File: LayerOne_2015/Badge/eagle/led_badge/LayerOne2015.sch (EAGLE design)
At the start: 72 parts, among them IC2 PQ1X331M2ZP-3V3-LDO-SOT-23-5, Q1 BSS138

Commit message: 
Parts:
- removed Q1: BSS138, SparkFun:MOSFET-NCHANNELSMD
- removed R5, R6: 10K, SparkFun:RESISTOR0805-RES
- added IC9: M74VHC1GT125DF2G, 74xx-little-de:74AHC1G125DCK
- added JP4: (no value), SparkFun:M07
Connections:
- removed net P1_5_5V: Q1.D, R6.2
- removed net P4_VDD: D1.C, IC2.VC, IC2.VIN, JP2.1, R6.1
- new net N$29: JP4.7, U$1.P0_0
- new net N$30: JP4.6, U$1.P0_1
- new net N$31: JP4.5, U$1.P0_2
- new net N$32: JP4.4, U$1.P0_3
- new net N$33: JP4.3, U$1.P0_4
- new net N$34: JP4.2, U$1.P0_5
- new net N$35: JP4.1, U$1.P0_6
- new net VCC: D1.C, IC2.VC, IC2.VIN, JP2.1
- net 3.3V: no longer Q1.G, R5.1
- net DIN: now also IC9A.O
- net GND: now also IC9A.OE
- net P1_5_3V: now also IC9A.I; no longer Q1.S, R5.2
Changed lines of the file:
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@@
 <?xml version="1.0" encoding="utf-8"?>
 <!DOCTYPE eagle SYSTEM "eagle.dtd">
-<eagle version="7.1.0">
+<eagle version="7.2.0">
 <drawing>
 <settings>
@@
 <part name="GND10" library="SparkFun-Aesthetics" deviceset="GND" device=""/>
 <part name="JP3" library="SparkFun-Connectors" deviceset="M05" device="PTH"/>
-<part name="Q1" library="SparkFun" deviceset="MOSFET-NCHANNEL" device="SMD" value="BSS138"/>
-<part name="R5" library="SparkFun" deviceset="RESISTOR" device="0805-RES" value="10K"/>
-<part name="R6" library="SparkFun" deviceset="RESISTOR" device="0805-RES" value="10K"/>
 <part name="BAT1" library="tvbgone-adj" deviceset="BATTERY" device="CR123A" value="CR123A"/>
 <part name="BAT2" library="tvbgone-adj" deviceset="BATTERY" device="CR123A" value="CR123A"/>
 <part name="GND12" library="supply1" deviceset="GND" device=""/>
 <part name="D1" library="SparkFun-DiscreteSemi" deviceset="DIODE" device="SMA"/>
+<part name="IC9" library="74xx-little-de" deviceset="74*1G125" device="DCK" technology="AHC" value="M74VHC1GT125DF2G ">
+<attribute name="DIGIKEY-ND" value="M74VHC1GT125DF1GOSCT-ND"/>
+<attribute name="MOUSER" value="863-M74VHC1GT125DF2G"/>
+<attribute name="PARTNO" value="M74VHC1GT125DF2G"/>
+</part>
+<part name="GND11" library="SparkFun-Aesthetics" deviceset="GND" device=""/>
+<part name="JP4" library="SparkFun" deviceset="M07" device=""/>
 </parts>
 <sheets>
@@
 <instance part="C23" gate="G$1" x="99.06" y="71.12"/>
 <instance part="GND1" gate="1" x="99.06" y="63.5"/>
-<instance part="C24" gate="G$1" x="124.46" y="40.64"/>
-<instance part="R1" gate="G$1" x="124.46" y="53.34" rot="R90"/>
-<instance part="GND2" gate="1" x="124.46" y="33.02"/>
+<instance part="C24" gate="G$1" x="134.62" y="40.64"/>
+<instance part="R1" gate="G$1" x="134.62" y="53.34" rot="R90"/>
+<instance part="GND2" gate="1" x="134.62" y="33.02"/>
 <instance part="C25" gate="G$1" x="119.38" y="78.74"/>
 <instance part="R2" gate="G$1" x="119.38" y="91.44" rot="R90"/>
@@
 <instance part="GND10" gate="1" x="25.4" y="68.58"/>
 <instance part="JP3" gate="G$1" x="-7.62" y="53.34"/>
-<instance part="Q1" gate="G$1" x="-15.24" y="-5.08" smashed="yes" rot="R270">
-<attribute name="NAME" x="-19.05" y="-0.254" size="1.778" layer="95"/>
-<attribute name="VALUE" x="-20.574" y="-10.668" size="1.778" layer="96"/>
-</instance>
-<instance part="R5" gate="G$1" x="-22.86" y="2.54" rot="R270"/>
-<instance part="R6" gate="G$1" x="-7.62" y="2.54" rot="R270"/>
 <instance part="BAT1" gate="G$1" x="-27.94" y="96.52" smashed="yes">
 <attribute name="NAME" x="-31.75" y="101.6" size="1.778" layer="95"/>
@@
 </instance>
 <instance part="D1" gate="G$1" x="-50.8" y="96.52" rot="R180"/>
+<instance part="IC9" gate="A" x="-25.4" y="0" smashed="yes">
+<attribute name="NAME" x="-22.86" y="3.175" size="1.778" layer="95"/>
+<attribute name="VALUE" x="-35.56" y="-7.62" size="1.778" layer="96"/>
+<attribute name="MOUSER" x="-25.4" y="0" size="1.778" layer="96" display="off"/>
+<attribute name="PARTNO" x="-25.4" y="0" size="1.778" layer="96" display="off"/>
+<attribute name="DIGIKEY-ND" x="-25.4" y="0" size="1.778" layer="96" display="off"/>
+</instance>
+<instance part="GND11" gate="1" x="-25.4" y="15.24" rot="R180"/>
+<instance part="JP4" gate="G$1" x="111.76" y="48.26" rot="R180"/>
 </instances>
 <busses>
@@
 <pinref part="C24" gate="G$1" pin="2"/>
 <pinref part="GND2" gate="1" pin="GND"/>
-<wire x1="124.46" y1="35.56" x2="124.46" y2="38.1" width="0.1524" layer="91"/>
+<wire x1="134.62" y1="35.56" x2="134.62" y2="38.1" width="0.1524" layer="91"/>
 </segment>
 <segment>
@@
 <pinref part="GND12" gate="1" pin="GND"/>
 </segment>
+<segment>
+<pinref part="IC9" gate="A" pin="OE"/>
+<pinref part="GND11" gate="1" pin="GND"/>
+<wire x1="-25.4" y1="12.7" x2="-25.4" y2="7.62" width="0.1524" layer="91"/>
+</segment>
 </net>
 <net name="GPIO2_3V" class="0">
@@
 <wire x1="0" y1="48.26" x2="7.62" y2="48.26" width="0.2032" layer="91"/>
 <label x="7.62" y="48.26" size="1.778" layer="95"/>
-</segment>
-<segment>
-<wire x1="-22.86" y1="7.62" x2="-22.86" y2="10.16" width="0.1524" layer="91"/>
-<wire x1="-22.86" y1="10.16" x2="-22.86" y2="12.7" width="0.1524" layer="91"/>
-<wire x1="-15.24" y1="2.54" x2="-15.24" y2="10.16" width="0.1524" layer="91"/>
-<wire x1="-15.24" y1="10.16" x2="-22.86" y2="10.16" width="0.1524" layer="91"/>
-<junction x="-22.86" y="10.16"/>
-<pinref part="R5" gate="G$1" pin="1"/>
-<pinref part="Q1" gate="G$1" pin="G"/>
-<label x="-22.86" y="12.7" size="1.778" layer="95" rot="R90"/>
 </segment>
 </net>
@@
 <pinref part="C24" gate="G$1" pin="1"/>
 <pinref part="R1" gate="G$1" pin="1"/>
-<wire x1="124.46" y1="48.26" x2="124.46" y2="45.72" width="0.1524" layer="91"/>
+<wire x1="134.62" y1="48.26" x2="134.62" y2="45.72" width="0.1524" layer="91"/>
 </segment>
 </net>
@@
 <segment>
 <pinref part="U$1" gate="G$1" pin="P4_3"/>
-<wire x1="86.36" y1="35.56" x2="93.98" y2="35.56" width="0.1524" layer="91"/>
-<label x="93.98" y="35.56" size="1.778" layer="95" xref="yes"/>
+<wire x1="86.36" y1="35.56" x2="88.9" y2="35.56" width="0.1524" layer="91"/>
+<label x="88.9" y="35.56" size="1.778" layer="95" xref="yes"/>
 </segment>
 </net>
@@
 <segment>
 <pinref part="R1" gate="G$1" pin="2"/>
-<wire x1="124.46" y1="58.42" x2="124.46" y2="60.96" width="0.1524" layer="91"/>
-<wire x1="124.46" y1="60.96" x2="116.84" y2="60.96" width="0.1524" layer="91"/>
+<wire x1="134.62" y1="58.42" x2="134.62" y2="60.96" width="0.1524" layer="91"/>
+<wire x1="134.62" y1="60.96" x2="116.84" y2="60.96" width="0.1524" layer="91"/>
 <label x="116.84" y="60.96" size="1.778" layer="95" rot="R180" xref="yes"/>
 </segment>
@@
 </segment>
 <segment>
-<pinref part="Q1" gate="G$1" pin="S"/>
-<wire x1="-20.32" y1="-5.08" x2="-22.86" y2="-5.08" width="0.1524" layer="91"/>
-<pinref part="R5" gate="G$1" pin="2"/>
-<wire x1="-22.86" y1="-5.08" x2="-30.48" y2="-5.08" width="0.1524" layer="91"/>
-<wire x1="-22.86" y1="-2.54" x2="-22.86" y2="-5.08" width="0.1524" layer="91"/>
-<junction x="-22.86" y="-5.08"/>
-<label x="-30.48" y="-5.08" size="1.27" layer="95" rot="R90" xref="yes"/>
+<wire x1="-30.48" y1="0" x2="-38.1" y2="0" width="0.1524" layer="91"/>
+<pinref part="IC9" gate="A" pin="I"/>
+<label x="-50.8" y="0" size="1.778" layer="95"/>
 </segment>
 </net>
@@
 </segment>
 </net>
-<net name="P4_VDD" class="0">
+<net name="VCC" class="0">
 <segment>
 <pinref part="IC2" gate="G$1" pin="VIN"/>
@@
 </segment>
 <segment>
-<wire x1="-7.62" y1="7.62" x2="-7.62" y2="12.7" width="0.1524" layer="91"/>
-<pinref part="R6" gate="G$1" pin="1"/>
-<label x="-7.62" y="12.7" size="1.778" layer="95" rot="R90"/>
-</segment>
-<segment>
 <pinref part="JP2" gate="G$1" pin="1"/>
 <wire x1="149.86" y1="40.64" x2="149.86" y2="33.02" width="0.2032" layer="91"/>
@@
 <wire x1="-55.88" y1="96.52" x2="-55.88" y2="81.28" width="0.2032" layer="91"/>
 <label x="-55.88" y="81.28" size="1.778" layer="95" rot="R270" xref="yes"/>
-</segment>
-</net>
-<net name="P1_5_5V" class="0">
-<segment>
-<pinref part="Q1" gate="G$1" pin="D"/>
-<wire x1="-10.16" y1="-5.08" x2="-7.62" y2="-5.08" width="0.1524" layer="91"/>
-<pinref part="R6" gate="G$1" pin="2"/>
-<wire x1="-7.62" y1="-5.08" x2="-5.08" y2="-5.08" width="0.1524" layer="91"/>
-<wire x1="-7.62" y1="-2.54" x2="-7.62" y2="-5.08" width="0.1524" layer="91"/>
-<junction x="-7.62" y="-5.08"/>
-<label x="-5.08" y="-5.08" size="1.27" layer="95" xref="yes"/>
 </segment>
 </net>
@@
 <label x="152.4" y="22.86" size="1.778" layer="95" rot="R270"/>
 </segment>
+<segment>
+<wire x1="-17.78" y1="0" x2="-10.16" y2="0" width="0.1524" layer="91"/>
+<pinref part="IC9" gate="A" pin="O"/>
+<label x="-10.16" y="0" size="1.778" layer="95"/>
+</segment>
+</net>
+<net name="N$29" class="0">
+<segment>
+<pinref part="U$1" gate="G$1" pin="P0_0"/>
+<wire x1="86.36" y1="38.1" x2="106.68" y2="38.1" width="0.1524" layer="91"/>
+<pinref part="JP4" gate="G$1" pin="7"/>
+</segment>
+</net>
+<net name="N$30" class="0">
+<segment>
+<pinref part="U$1" gate="G$1" pin="P0_1"/>
+<wire x1="86.36" y1="40.64" x2="106.68" y2="40.64" width="0.1524" layer="91"/>
+<pinref part="JP4" gate="G$1" pin="6"/>
+</segment>
+</net>
+<net name="N$31" class="0">
+<segment>
+<pinref part="U$1" gate="G$1" pin="P0_2"/>
+<wire x1="86.36" y1="43.18" x2="106.68" y2="43.18" width="0.1524" layer="91"/>
+<pinref part="JP4" gate="G$1" pin="5"/>
+</segment>
+</net>
+<net name="N$32" class="0">
+<segment>
+<pinref part="U$1" gate="G$1" pin="P0_3"/>
+<wire x1="86.36" y1="45.72" x2="106.68" y2="45.72" width="0.1524" layer="91"/>
+<pinref part="JP4" gate="G$1" pin="4"/>
+</segment>
+</net>
+<net name="N$33" class="0">
+<segment>
+<pinref part="U$1" gate="G$1" pin="P0_4"/>
+<wire x1="86.36" y1="48.26" x2="106.68" y2="48.26" width="0.1524" layer="91"/>
+<pinref part="JP4" gate="G$1" pin="3"/>
+</segment>
+</net>
+<net name="N$34" class="0">
+<segment>
+<pinref part="U$1" gate="G$1" pin="P0_5"/>
+<wire x1="86.36" y1="50.8" x2="106.68" y2="50.8" width="0.1524" layer="91"/>
+<pinref part="JP4" gate="G$1" pin="2"/>
+</segment>
+</net>
+<net name="N$35" class="0">
+<segment>
+<pinref part="U$1" gate="G$1" pin="P0_6"/>
+<wire x1="86.36" y1="53.34" x2="106.68" y2="53.34" width="0.1524" layer="91"/>
+<pinref part="JP4" gate="G$1" pin="1"/>
+</segment>
 </net>
 </nets>
 </sheet>
-<sheet>
-<plain>
-</plain>
-<instances>
-</instances>
-<busses>
-</busses>
-<nets>
-</nets>
-</sheet>

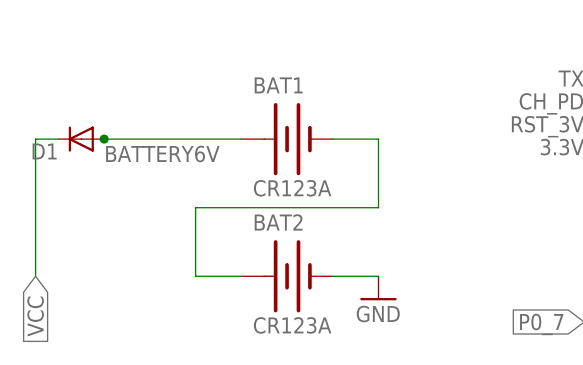
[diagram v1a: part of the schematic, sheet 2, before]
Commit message: 
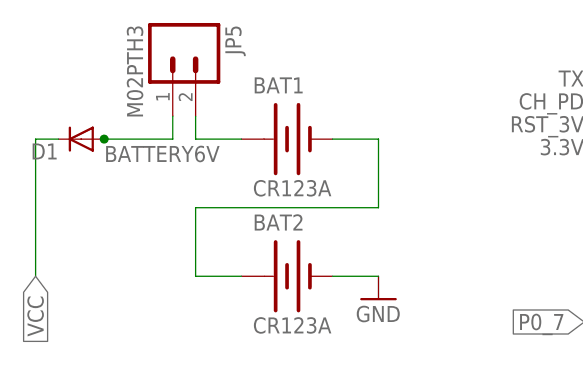
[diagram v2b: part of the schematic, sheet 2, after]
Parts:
- added JP5: M02PTH3, SparkFun-Connectors:M02PTH3
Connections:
- removed net VDD: C1.1, C10.1, C11.1, C12.1, C13.1, C14.1, C15.1, C16.1, C17.1, C18.1, C19.1, C2.1, C20.1, C21.1, C22.1, C3.1, C4.1, C5.1, C6.1, C7.1, C8.1, C9.1, L1.VDD, L10.VDD, L11.VDD, L12.VDD, L13.VDD, L14.VDD, L15.VDD, L16.VDD, L17.VDD, L18.VDD, L19.VDD, L2.VDD, L20.VDD, L21.VDD, L22.VDD, L3.VDD, L4.VDD, L5.VDD, L6.VDD, L7.VDD, L8.VDD, L9.VDD
- new net N$36: BAT1.+, JP5.2
- net BATTERY6V: now also JP5.1; no longer BAT1.+
- net VCC: now also C1.1, C10.1, C11.1, C12.1, C13.1, C14.1, C15.1, C16.1, C17.1, C18.1, C19.1, C2.1, C20.1, C21.1, C22.1, C3.1, C4.1, C5.1, C6.1, C7.1, C8.1, C9.1, L1.VDD, L10.VDD, L11.VDD, L12.VDD, L13.VDD, L14.VDD, L15.VDD, L16.VDD, L17.VDD, L18.VDD, L19.VDD, L2.VDD, L20.VDD, L21.VDD, L22.VDD, L3.VDD, L4.VDD, L5.VDD, L6.VDD, L7.VDD, L8.VDD, L9.VDD
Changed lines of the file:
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@@
 <part name="GND11" library="SparkFun-Aesthetics" deviceset="GND" device=""/>
 <part name="JP4" library="SparkFun" deviceset="M07" device=""/>
+<part name="JP5" library="SparkFun-Connectors" deviceset="M02" device="PTH3"/>
 </parts>
 <sheets>
@@
 </segment>
 </net>
-<net name="VDD" class="0">
+<net name="N$19" class="0">
+<segment>
+<pinref part="L22" gate="G$1" pin="DOUT"/>
+<pinref part="JP1-DOUT" gate="G$1" pin="1"/>
+<wire x1="25.4" y1="7.62" x2="43.18" y2="7.62" width="0.2032" layer="91"/>
+</segment>
+</net>
+<net name="N$25" class="0">
+<segment>
+<pinref part="L10" gate="G$1" pin="DOUT"/>
+<wire x1="152.4" y1="83.82" x2="157.48" y2="83.82" width="0.2032" layer="91"/>
+<wire x1="157.48" y1="83.82" x2="157.48" y2="66.04" width="0.2032" layer="91"/>
+<wire x1="157.48" y1="66.04" x2="-10.16" y2="66.04" width="0.2032" layer="91"/>
+<wire x1="-10.16" y1="66.04" x2="-10.16" y2="45.72" width="0.2032" layer="91"/>
+<pinref part="L11" gate="G$1" pin="DIN"/>
+<wire x1="-10.16" y1="45.72" x2="-2.54" y2="45.72" width="0.2032" layer="91"/>
+</segment>
+</net>
+<net name="N$26" class="0">
+<segment>
+<pinref part="L20" gate="G$1" pin="DOUT"/>
+<wire x1="152.4" y1="45.72" x2="154.94" y2="45.72" width="0.2032" layer="91"/>
+<wire x1="154.94" y1="45.72" x2="154.94" y2="27.94" width="0.2032" layer="91"/>
+<wire x1="154.94" y1="27.94" x2="-7.62" y2="27.94" width="0.2032" layer="91"/>
+<wire x1="-7.62" y1="27.94" x2="-7.62" y2="7.62" width="0.2032" layer="91"/>
+<pinref part="L21" gate="G$1" pin="DIN"/>
+<wire x1="-7.62" y1="7.62" x2="-2.54" y2="7.62" width="0.2032" layer="91"/>
+</segment>
+</net>
+<net name="N$27" class="0">
+<segment>
+<pinref part="L3" gate="G$1" pin="DIN"/>
+<pinref part="L2" gate="G$1" pin="DOUT"/>
+<wire x1="25.4" y1="83.82" x2="33.02" y2="83.82" width="0.2032" layer="91"/>
+</segment>
+</net>
+<net name="VCC" class="0">
 <segment>
 <pinref part="L1" gate="G$1" pin="VDD"/>
@@
 <pinref part="SUPPLY65" gate="G$1" pin="VDD"/>
 <pinref part="L22" gate="G$1" pin="VDD"/>
-</segment>
-</net>
-<net name="N$19" class="0">
-<segment>
-<pinref part="L22" gate="G$1" pin="DOUT"/>
-<pinref part="JP1-DOUT" gate="G$1" pin="1"/>
-<wire x1="25.4" y1="7.62" x2="43.18" y2="7.62" width="0.2032" layer="91"/>
-</segment>
-</net>
-<net name="N$25" class="0">
-<segment>
-<pinref part="L10" gate="G$1" pin="DOUT"/>
-<wire x1="152.4" y1="83.82" x2="157.48" y2="83.82" width="0.2032" layer="91"/>
-<wire x1="157.48" y1="83.82" x2="157.48" y2="66.04" width="0.2032" layer="91"/>
-<wire x1="157.48" y1="66.04" x2="-10.16" y2="66.04" width="0.2032" layer="91"/>
-<wire x1="-10.16" y1="66.04" x2="-10.16" y2="45.72" width="0.2032" layer="91"/>
-<pinref part="L11" gate="G$1" pin="DIN"/>
-<wire x1="-10.16" y1="45.72" x2="-2.54" y2="45.72" width="0.2032" layer="91"/>
-</segment>
-</net>
-<net name="N$26" class="0">
-<segment>
-<pinref part="L20" gate="G$1" pin="DOUT"/>
-<wire x1="152.4" y1="45.72" x2="154.94" y2="45.72" width="0.2032" layer="91"/>
-<wire x1="154.94" y1="45.72" x2="154.94" y2="27.94" width="0.2032" layer="91"/>
-<wire x1="154.94" y1="27.94" x2="-7.62" y2="27.94" width="0.2032" layer="91"/>
-<wire x1="-7.62" y1="27.94" x2="-7.62" y2="7.62" width="0.2032" layer="91"/>
-<pinref part="L21" gate="G$1" pin="DIN"/>
-<wire x1="-7.62" y1="7.62" x2="-2.54" y2="7.62" width="0.2032" layer="91"/>
-</segment>
-</net>
-<net name="N$27" class="0">
-<segment>
-<pinref part="L3" gate="G$1" pin="DIN"/>
-<pinref part="L2" gate="G$1" pin="DOUT"/>
-<wire x1="25.4" y1="83.82" x2="33.02" y2="83.82" width="0.2032" layer="91"/>
 </segment>
 </net>
@@
 <instance part="GND11" gate="1" x="-25.4" y="15.24" rot="R180"/>
 <instance part="JP4" gate="G$1" x="111.76" y="48.26" rot="R180"/>
+<instance part="JP5" gate="G$1" x="-40.64" y="106.68" rot="R270"/>
 </instances>
 <busses>
@@
 <net name="BATTERY6V" class="0">
 <segment>
-<pinref part="BAT1" gate="G$1" pin="+"/>
-<wire x1="-33.02" y1="96.52" x2="-48.26" y2="96.52" width="0.1524" layer="91"/>
+<wire x1="-40.64" y1="99.06" x2="-40.64" y2="96.52" width="0.1524" layer="91"/>
+<wire x1="-40.64" y1="96.52" x2="-48.26" y2="96.52" width="0.1524" layer="91"/>
 <label x="-48.26" y="93.98" size="1.778" layer="95"/>
 <junction x="-48.26" y="96.52"/>
 <pinref part="D1" gate="G$1" pin="A"/>
+<pinref part="JP5" gate="G$1" pin="1"/>
 </segment>
 </net>
@@
 </segment>
 </net>
+<net name="N$36" class="0">
+<segment>
+<pinref part="BAT1" gate="G$1" pin="+"/>
+<wire x1="-33.02" y1="96.52" x2="-38.1" y2="96.52" width="0.1524" layer="91"/>
+<wire x1="-38.1" y1="96.52" x2="-38.1" y2="99.06" width="0.1524" layer="91"/>
+<pinref part="JP5" gate="G$1" pin="2"/>
+</segment>
+</net>
